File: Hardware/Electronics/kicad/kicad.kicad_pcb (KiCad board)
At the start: 2 copper layers, 28 x 130 mm, 47 parts, among them J1 Conn_01x03_Socket, J2 Conn_01x03_Socket, J3 Conn_01x03_Socket, J6 USB_C_Receptacle_USB2.0_16P, SW1 SW_Push, SW2 SW_Push, SW3 SW_Push, U1 USBLC6-2P6, U2 MCP73831-2-OT, U3 ESP32-C3-MINI-1-N4, U4 XC6210B332MR, U5 TPS61023DRLR, U6 SN74LV1T34DBV

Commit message: PCB Tweaks
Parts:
- C11: value 0.1u -> 100n
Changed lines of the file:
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@@
     (descr "Capacitor SMD 0805 (2012 Metric), square (rectangular) end terminal, IPC_7351 nominal, (Body size source: IPC-SM-782 page 76, https://www.pcb-3d.com/wordpress/wp-content/uploads/ipc-sm-782a_amendment_1_and_2.pdf, https://docs.google.com/spreadsheets/d/1BsfQQcO9C6DZCsRaXUlFlo91Tg2WpOkGARC1WS5S8t0/edit?usp=sharing), generated with kicad-footprint-generator")
     (tags "capacitor")
-    (property "LCSC" "C1744")
+    (property "LCSC" "C123621")
     (property "Sheetfile" "kicad.kicad_sch")
     (property "Sheetname" "")
@@
     (descr "Capacitor SMD 0805 (2012 Metric), square (rectangular) end terminal, IPC_7351 nominal, (Body size source: IPC-SM-782 page 76, https://www.pcb-3d.com/wordpress/wp-content/uploads/ipc-sm-782a_amendment_1_and_2.pdf, https://docs.google.com/spreadsheets/d/1BsfQQcO9C6DZCsRaXUlFlo91Tg2WpOkGARC1WS5S8t0/edit?usp=sharing), generated with kicad-footprint-generator")
     (tags "capacitor")
-    (property "LCSC" "C1744")
+    (property "LCSC" "C123621")
     (property "Sheetfile" "kicad.kicad_sch")
     (property "Sheetname" "")
@@
     (descr "Capacitor SMD 0805 (2012 Metric), square (rectangular) end terminal, IPC_7351 nominal, (Body size source: IPC-SM-782 page 76, https://www.pcb-3d.com/wordpress/wp-content/uploads/ipc-sm-782a_amendment_1_and_2.pdf, https://docs.google.com/spreadsheets/d/1BsfQQcO9C6DZCsRaXUlFlo91Tg2WpOkGARC1WS5S8t0/edit?usp=sharing), generated with kicad-footprint-generator")
     (tags "capacitor")
-    (property "LCSC" "C5120075")
+    (property "LCSC" "C83055")
     (property "Sheetfile" "kicad.kicad_sch")
     (property "Sheetname" "")
@@
         (effects (font (size 1 1) (thickness 0.15)))
     )
-    (fp_text value "0.1u" (at 0 1.68) (layer "F.Fab")
+    (fp_text value "100n" (at 0 1.68) (layer "F.Fab")
         (effects (font (size 1 1) (thickness 0.15)))
     )
@@
     (descr "http://industrial.panasonic.com/cdbs/www-data/pdf/ATV0000/ATV0000CE5.pdf")
     (tags "SMD SMT SPST EVQPUL EVQPUC")
-    (property "LCSC" "C79174")
-    (property "Sheetfile" "kicad.kicad_sch")
-    (property "Sheetname" "")
+    (property "LCSC" "C397351")
+    (property "Sheetfile" "kicad.kicad_sch")
+    (property "Sheetname" "")

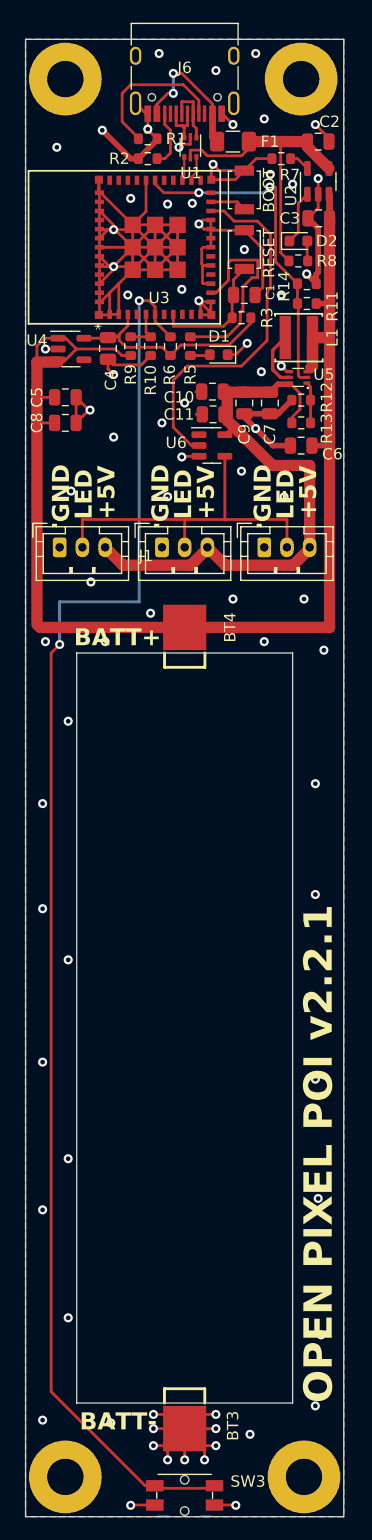
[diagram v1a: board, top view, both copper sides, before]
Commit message: Add KiCad MCP configuration and new script for editing schematic text
- Introduced a new MCP configuration file for KiCad.
- Added a Python script to automate the editing of schematic text, including functionality for managing component instances and labels.
- Updated the platformio.ini to streamline the default environment settings.
- Adjusted firmware BLE handling for pattern saving and button state management.
- Modified LED handling to support multiple strips and improved brightness control.
- Updated KiCad PCB files and removed obsolete autosave files.
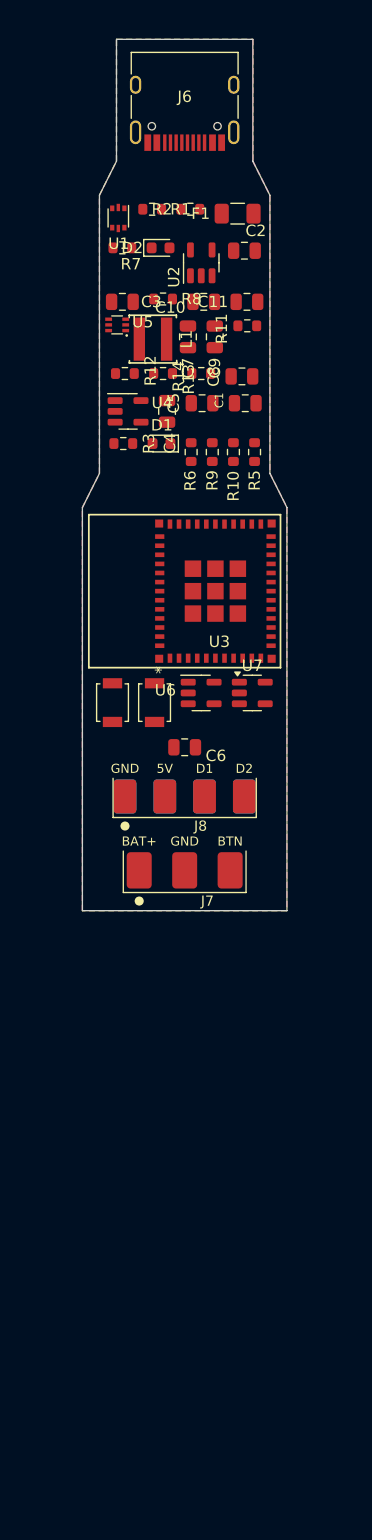
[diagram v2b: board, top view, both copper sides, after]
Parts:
- removed BT3, BT4: MY-ZJ-110, easyeda2kicad:SMD_MY-ZJ-110
- removed H1, H2, H3, H4: MountingHole, MountingHole:MountingHole_3.2mm_M3_Pad
- removed J1, J2, J3: Conn_01x03_Socket, Connector_JST:JST_PH_B3B-PH-K_1x03_P2.00mm_Vertical
- removed SW3: SW_Push, Button_Switch_SMD:Panasonic_EVQPUL_EVQPUC
- added J7: PWR_BTN, custom_footprints:Power_Button_SolderPads_1x03, F.Cu at (64.0, 103.1)
- added J8: LED, custom_footprints:LED_Strip_SolderPads_1x04, F.Cu at (64.0, 96.6)
- added J9: LED, custom_footprints:LED_Strip_SolderPads_1x04, B.Cu at (64.0, 96.6)
- added U7: SN74LV1T34DBV, Package_TO_SOT_SMD:SOT-23-5, F.Cu at (70.0, 87.5)
- moved SW2 45.8 mm to (61.4, 88.4)
- moved SW1 41.5 mm to (57.6, 88.4)
- moved U3 30.7 mm to (64.0, 78.6)
- moved C6 28.5 mm to (64.0, 92.3)
- moved U6 21.8 mm to (65.5, 87.5)
- moved C3 18.8 mm to (58.5, 53.1)
- moved U5 16.6 mm to (58.1, 55.1)
- moved C8 16.1 mm to (69.0, 59.7)
- moved R7 16.0 mm to (58.5, 48.4)
- moved R12 15.7 mm to (58.7, 59.4)
- moved R3 15.2 mm to (58.6, 65.6)
- moved R13 12.9 mm to (62.1, 59.4)
- moved L1 12.8 mm to (61.2, 56.4)
- moved U2 12.5 mm to (65.5, 49.7)
- moved R8 12.4 mm to (62.1, 52.9)
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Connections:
- U6 pad 4: Net-(J1-Pin_2) -> LED1
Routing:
- net -BATT: track 222.9 -> 0.00 mm, vias 77 -> 0
- net POI SW: track 126.1 -> 0.00 mm, vias 2 -> 0
- net +BATT: track 111.5 -> 0.00 mm
- net +5V: track 49.9 -> 0.00 mm
- net LED Data: track 32.3 -> 0.00 mm
- net Net-(J1-Pin_2): track 30.9 -> 0.00 mm
- net REG_SIGNAL: track 29.4 -> 0.00 mm, vias 2 -> 0
- net +5VD: track 26.0 -> 0.00 mm
- net +3.3V: track 19.6 -> 0.00 mm
- net ESP LED: track 17.6 -> 0.00 mm
- net Net-(J6-CC1): track 13.4 -> 0.00 mm
- net Net-(F1-Pad1): track 12.5 -> 0.00 mm, vias 2 -> 0
- net RESET: track 11.3 -> 0.00 mm
- net Net-(J6-D--PadA7): track 5.31 -> 0.00 mm
- net Net-(U5-SW): track 5.05 -> 0.00 mm
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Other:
- board size 28 x 130 mm -> 18 x 76.7 mm
- board text removed: "+5V"
- board text removed: "BATT+"
- board text removed: "BATT-"
- board text removed: "BOOT"
- board text removed: "GND"
- board text removed: "I created this project to provide a cheap yet capable poi option to the community. It has a simple set of functionality to keep the focus on use and spinning. It is fully open souce and intended to be DIY, to encourage making, and full ownership of our technology. Suggested donation of 5$ per set of poi built via paypal. Link is available at github.com/mitchlol/Open-Pixel-Poi along with all the s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"
- board text removed: "LED"
- board text removed: "OPEN PIXEL POI v2.2.1"
- board text removed: "RESET"
